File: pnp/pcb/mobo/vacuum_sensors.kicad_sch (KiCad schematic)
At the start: 18 parts, among them J33 I2C_AUX, U2 XGZP6857D, U3 XGZP6857D, U4 PCA9545A

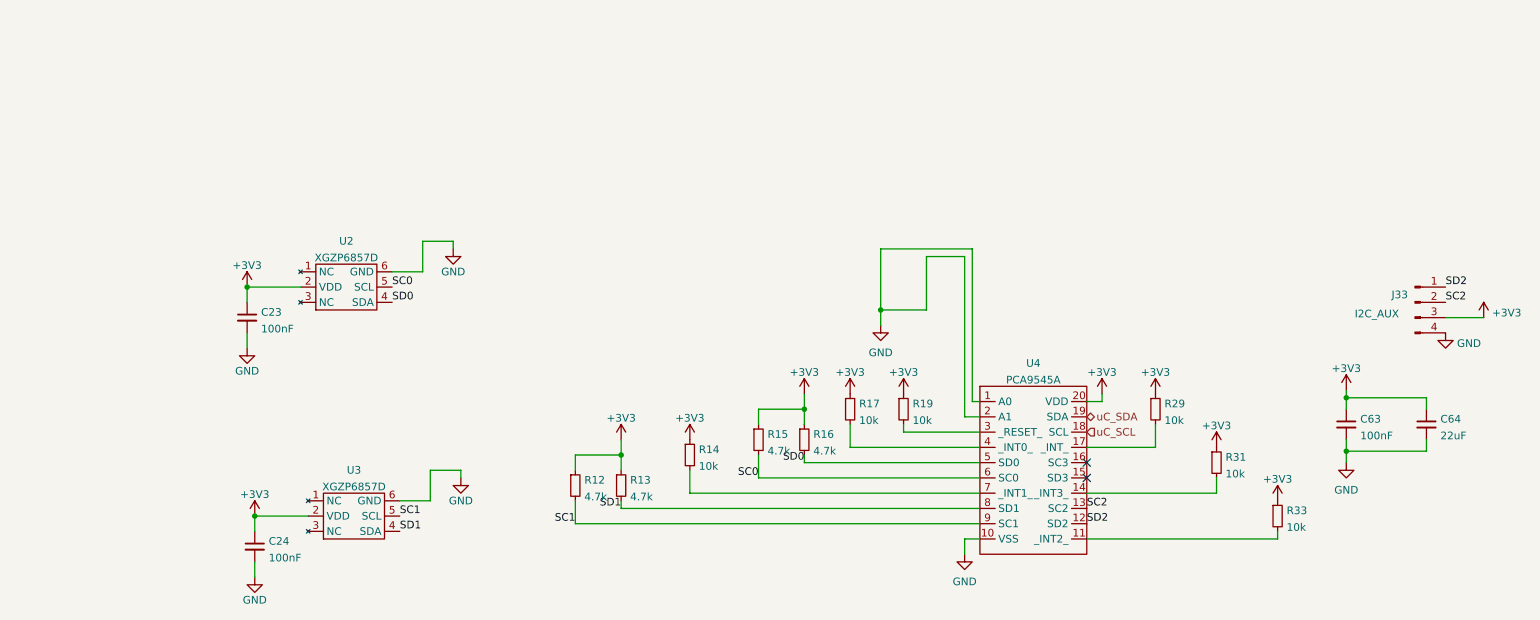
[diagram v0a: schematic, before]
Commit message: Update mobo schematic with part numbers and ratings
All parts now have part numbers for at least one reseller or manufacturer along with rating specifications.

Note: I did not update the PCB with these new properties, as it seems the PCB is a bit out of sync with the schematic.
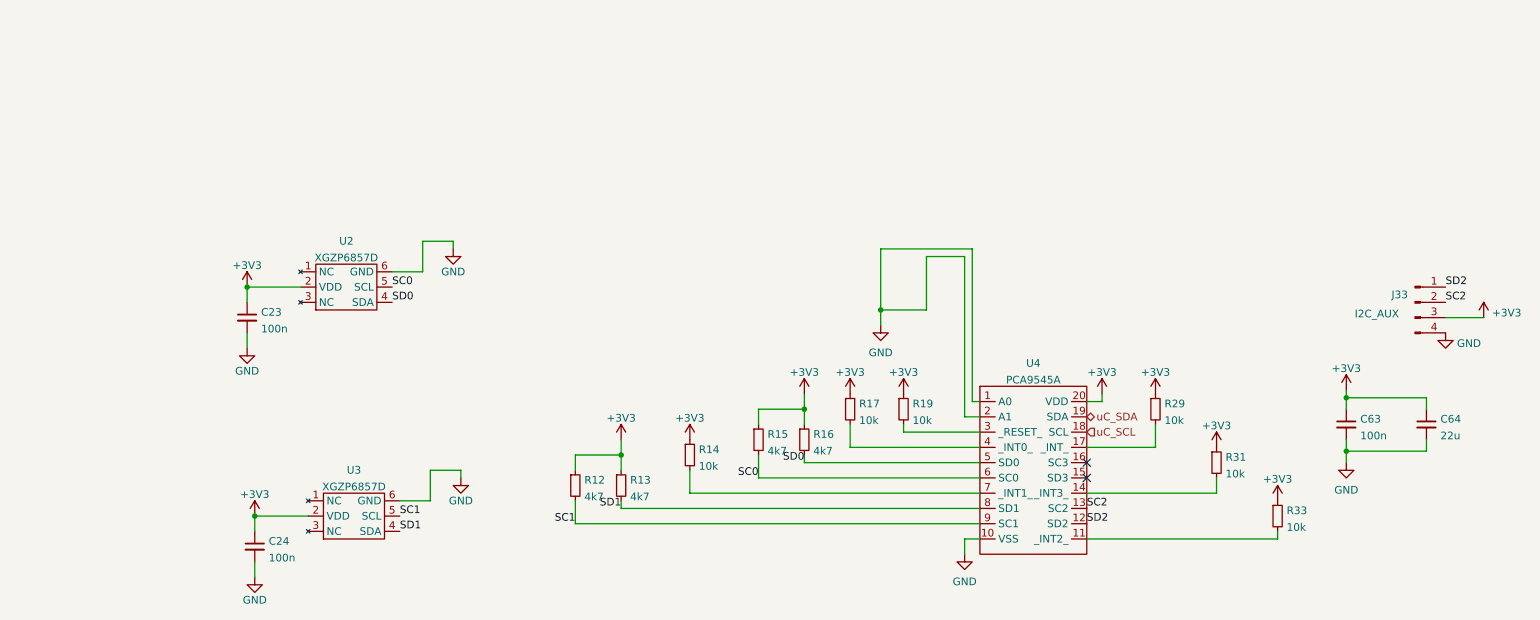
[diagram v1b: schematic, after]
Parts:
- C23, C24, C63: value 100nF -> 100n; Digikey (none) -> 1276-1180-1-ND; JLCPCB (none) -> C49678; LCSC (none) -> C360619; Mouser (none) -> 581-08055C104K; Notes (none) -> 50V/10%
- C64: value 22uF -> 22u; JLCPCB (none) -> C45783; LCSC (none) -> C5674; Notes (none) -> 25V/20%
- R12, R13, R15, R16: value 4.7k -> 4k7; Digikey (none) -> A129757CT-ND; JLCPCB (none) -> C17673; LCSC (none) -> C17673; Mouser (none) -> 71-CRCW08054K70FKEAC; Notes (none) -> 125mW/1%
- R14, R17, R19, R29, R31, R33: Digikey (none) -> RMCF0805FT10K0CT-ND; JLCPCB (none) -> C17414; LCSC (none) -> C115295; Mouser (none) -> 71-CRCW080510K0FKEAC; Notes (none) -> 125mW/1%
- U2, U3: Notes (none) -> Must at least cover 0 - 1 bar / 0 - 0.1 MPa / 0 - 15 PSI
- U4: Digikey (none) -> 568-1865-1-ND

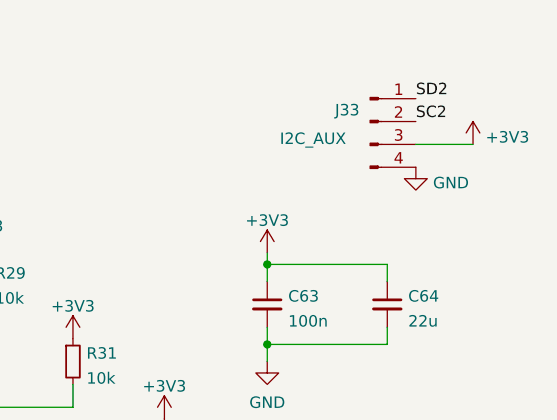
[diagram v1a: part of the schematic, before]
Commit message: adds tons of TVS and inline resistors
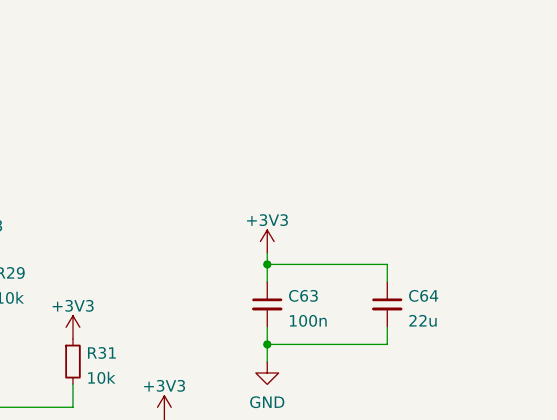
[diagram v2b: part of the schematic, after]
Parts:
- removed J33: I2C_AUX, Connector_PinHeader_2.54mm:PinHeader_1x04_P2.54mm_Vertical, symbol Connector:Conn_01x04_Male
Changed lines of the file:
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@@
-    (stroke (width 0) (type default))
-  )
-  (wire (pts (xy 261.62 88.9) (xy 267.97 88.9))
     (stroke (width 0) (type default))
   )
@@
     (effects (font (size 1.27 1.27)) (justify left bottom))
   )
-  (label "SD2" (at 261.62 83.82 0) (fields_autoplaced)
-    (effects (font (size 1.27 1.27)) (justify left bottom))
-  )
-  (label "SC2" (at 261.62 86.36 0) (fields_autoplaced)
-    (effects (font (size 1.27 1.27)) (justify left bottom))
-  )
   (label "SD0" (at 86.36 86.36 0) (fields_autoplaced)
     (effects (font (size 1.27 1.27)) (justify left bottom))
@@
     (effects (font (size 1.27 1.27)) (justify left))
   )
-  (symbol (lib_id "power:+3V3") (at 267.97 88.9 0) (unit 1)
-    (in_bom yes) (on_board yes) (dnp no) (fields_autoplaced)
-    (property "Reference" "#PWR0250" (at 267.97 92.71 0)
-      (effects (font (size 1.27 1.27)) hide)
-    )
-    (property "Value" "+3V3" (at 269.367 88.109 0)
-      (effects (font (size 1.27 1.27)) (justify left))
-    )
-    (property "Footprint" "" (at 267.97 88.9 0)
-      (effects (font (size 1.27 1.27)) hide)
-    )
-    (property "Datasheet" "" (at 267.97 88.9 0)
-      (effects (font (size 1.27 1.27)) hide)
-    )
-    (pin "1")
-    (instances
-      (project "mobo"
-        (path "/7255cbd1-8d38-4545-be9a-7fc5488ef942/00000000-0000-0000-0000-00005eb0c5a0"
-          (reference "#PWR0250") (unit 1)
-        )
-      )
-    )
-  )
   (symbol (lib_id "power:+3V3") (at 171.45 101.6 0) (unit 1)
     (in_bom yes) (on_board yes) (dnp no) (fields_autoplaced)
@@
         (path "/7255cbd1-8d38-4545-be9a-7fc5488ef942/00000000-0000-0000-0000-00005eb0c5a0"
           (reference "#PWR0241") (unit 1)
-        )
-      )
-    )
-  )
-  (symbol (lib_id "Connector:Conn_01x04_Male") (at 256.54 86.36 0) (unit 1)
-    (in_bom yes) (on_board yes) (dnp no)
-    (property "Reference" "J33" (at 254 85.09 0)
-      (effects (font (size 1.27 1.27)))
-    )
-    (property "Value" "I2C_AUX" (at 250.19 88.265 0)
-      (effects (font (size 1.27 1.27)))
-    )
-    (property "Footprint" "Connector_PinHeader_2.54mm:PinHeader_1x04_P2.54mm_Vertical" (at 256.54 86.36 0)
-      (effects (font (size 1.27 1.27)) hide)
-    )
-    (property "Datasheet" "~" (at 256.54 86.36 0)
-      (effects (font (size 1.27 1.27)) hide)
-    )
-    (pin "1")
-    (pin "2")
-    (pin "3")
-    (pin "4")
-    (instances
-      (project "mobo"
-        (path "/7255cbd1-8d38-4545-be9a-7fc5488ef942/00000000-0000-0000-0000-00005eb0c5a0"
-          (reference "J33") (unit 1)
         )
       )
@@
         )
       )
-    )
-  )
-  (symbol (lib_id "power:GND") (at 261.62 91.44 0) (unit 1)
-    (in_bom yes) (on_board yes) (dnp no) (fields_autoplaced)
-    (property "Reference" "#PWR0249" (at 261.62 97.79 0)
-      (effects (font (size 1.27 1.27)) hide)
-    )
-    (property "Value" "GND" (at 263.525 93.189 0)
-      (effects (font (size 1.27 1.27)) (justify left))
-    )
-    (property "Footprint" "" (at 261.62 91.44 0)
-      (effects (font (size 1.27 1.27)) hide)
-    )
-    (property "Datasheet" "" (at 261.62 91.44 0)
-      (effects (font (size 1.27 1.27)) hide)
-    )
-    (pin "1")
-    (instances
-      (project "mobo"
-        (path "/7255cbd1-8d38-4545-be9a-7fc5488ef942/00000000-0000-0000-0000-00005eb0c5a0"
-          (reference "#PWR0249") (unit 1)
-        )
-      )

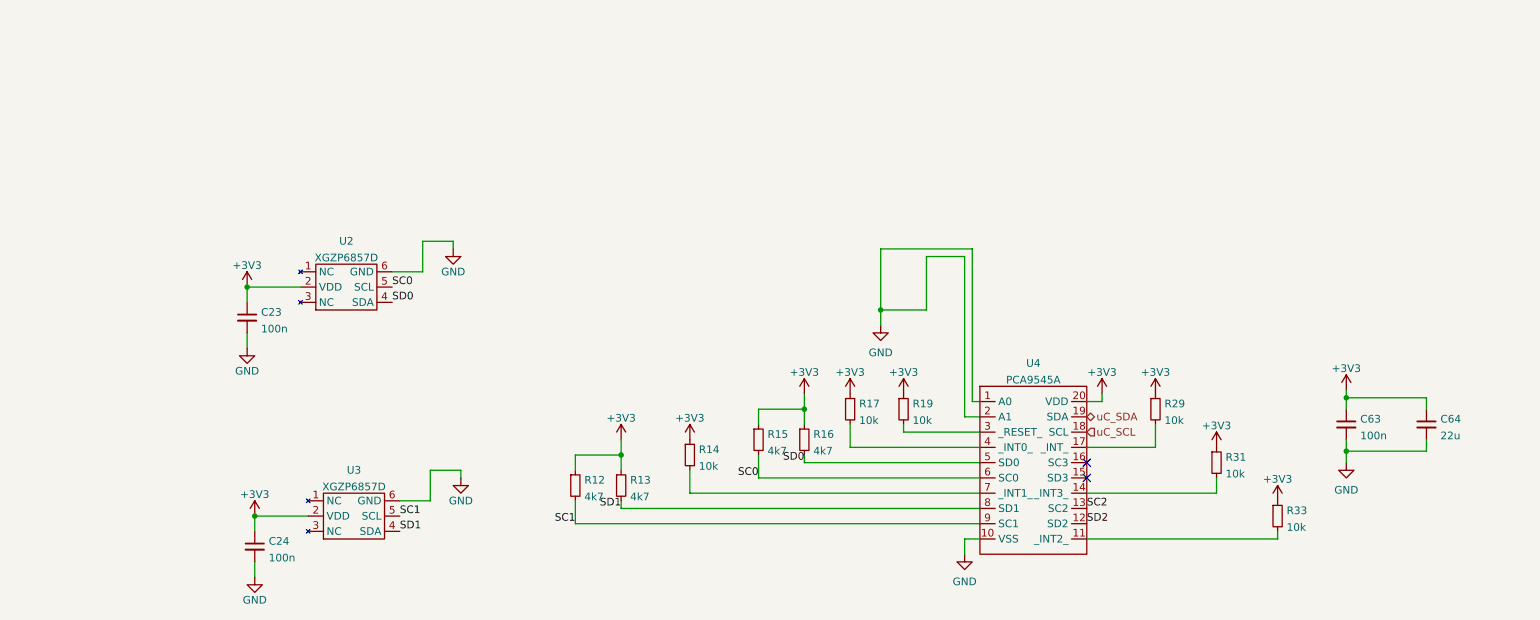
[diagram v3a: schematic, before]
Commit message: Updated symbols and changed I2C multiplexer to a simpler one
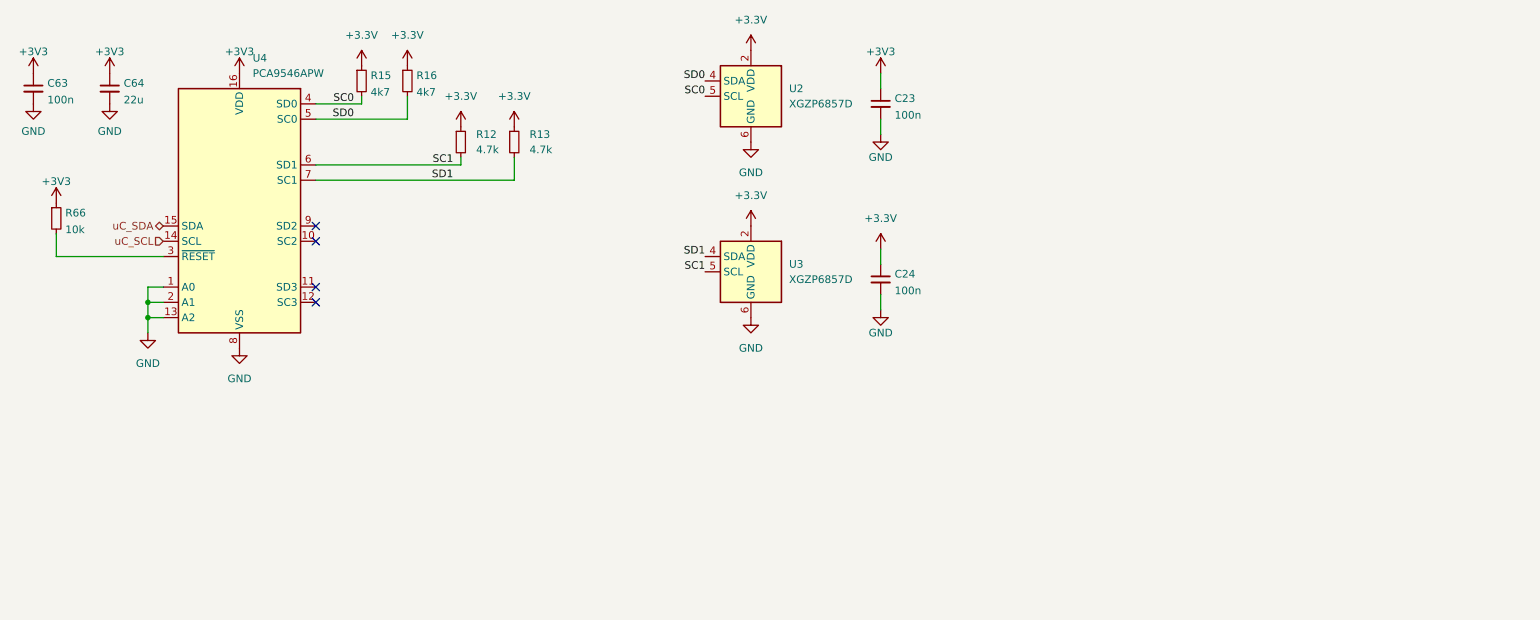
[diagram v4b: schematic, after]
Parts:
- removed R14, R17, R19, R29, R31, R33: 10k, Resistor_SMD:R_0805_2012Metric, symbol Device:R_Small
- removed U4: PCA9545A, Package_SO:TSSOP-20_4.4x6.5mm_P0.65mm, symbol index:PCA9545A
- added R66: 10k, Resistor_SMD:R_0805_2012Metric, symbol Device:R_Small
- added U4: PCA9546APW, Package_SO:TSSOP-16_4.4x5mm_P0.65mm, symbol index:PCA9546APW
- R12, R13: value 4k7 -> 4.7k
- U2, U3: footprint index:XGZP6857D -> Package_DIP:DIP-6_W10.16mm; Notes Must at least cover 0 - 1 bar / 0 - 0.1 MPa / 0 - 15 PSI -> (none)
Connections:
- net +3V3: now also R66.1, U4.16 (VDD); no longer C24.1, R12.1, R13.1, R15.1, R16.1, U2.2 (VDD), U3.2 (VDD)
- net GND: now also U4.1 (A0), U4.13 (A2), U4.2 (A1), U4.8 (VSS)
- net SC0: now also U4.4 (SD0)
- net SC1: now also U4.6 (SD1)
- net SD0: now also U4.5 (SC0)
- net SD1: now also U4.7 (SC1)
- net uC_SCL: now also U4.14 (SCL)
- net uC_SDA: now also U4.15 (SDA)
- new net: R66.2, U4.3 (~{RESET})
- new net +3.3V: C24.1, R12.1, R13.1, R15.1, R16.1, U2.2 (VDD), U3.2 (VDD)
- no-connect marks 2 -> 4
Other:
- moved on the sheet: C23, C24, C63, C64, R12, R13

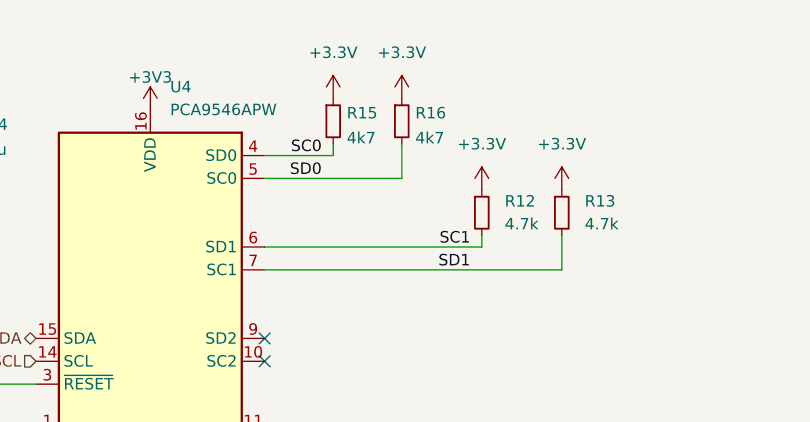
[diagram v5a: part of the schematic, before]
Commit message: Move level shifting from ringlight to mobo
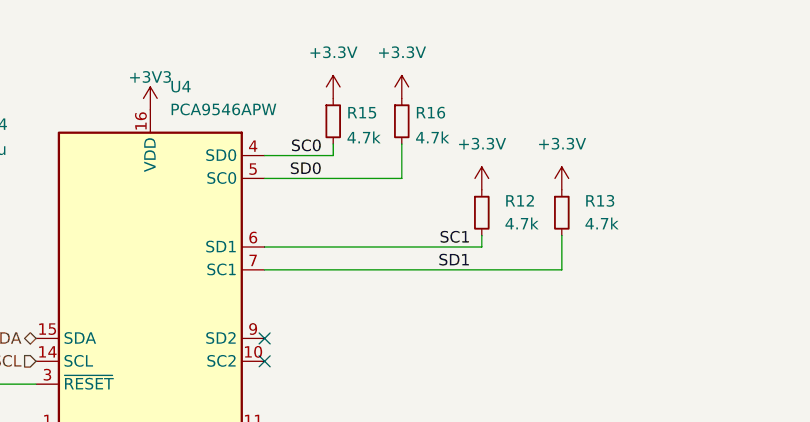
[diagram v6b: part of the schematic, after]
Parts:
- R15, R16: value 4k7 -> 4.7k
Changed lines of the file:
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@@
       (effects (font (size 1.27 1.27)) (justify left))
     )
-    (property "Value" "4k7" (at 90.3986 51.3966 0)
+    (property "Value" "4.7k" (at 90.3986 51.3966 0)
       (effects (font (size 1.27 1.27)) (justify left))
     )
@@
       (effects (font (size 1.27 1.27)) (justify left))
     )
-    (property "Value" "4k7" (at 82.7786 51.3966 0)
-      (effects (font (size 1.27 1.27)) (justify left))
-    )
+    (property "Value" "4.7k" (at 82.7786 51.3966 0)
+      (effects (font (size 1.27 1.27)) (justify left))
+    )

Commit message: Mobo parts sourced
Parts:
- C23, C24, C63: Digikey 1276-1180-1-ND -> (none); LCSC C360619 -> C476766; Mouser 581-08055C104K -> (none); Notes 50V/10% -> 6.3V
- C64: JLCPCB C45783 -> C1729; LCSC C5674 -> C107147; Notes 25V/20% -> 6.3V
- R12, R13, R15, R16: Notes 125mW/1% -> (none)
- R66: LCSC C115295 -> C17414; Notes 125mW/1% -> (none)
- U2, U3: JLCPCB (none) -> C3038044; LCSC (none) -> C3038044
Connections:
- net +3V3 is gone; now on net +3.3V: C23.1, C63.1, C64.1, R66.1, U4.16 (VDD)

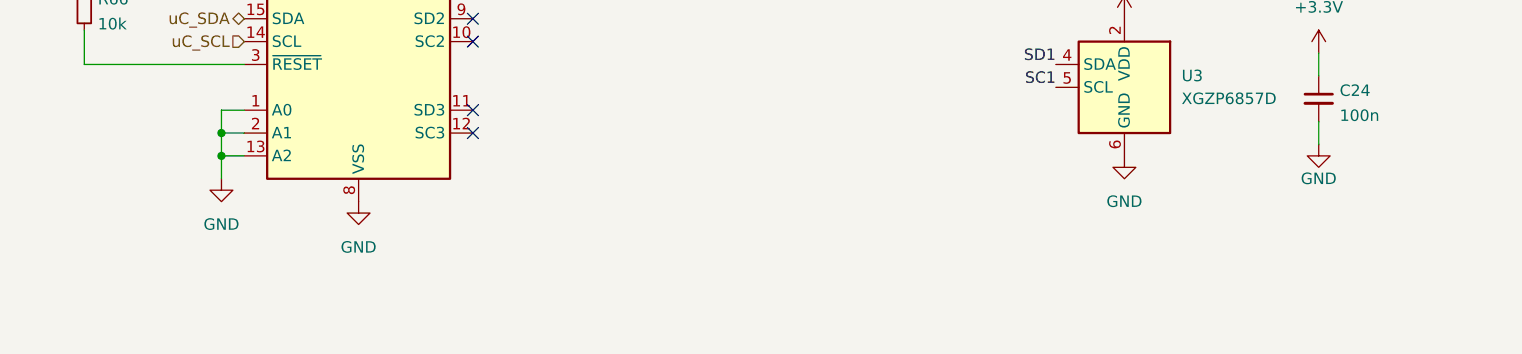
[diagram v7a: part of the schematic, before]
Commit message: Add notes to pending symbols
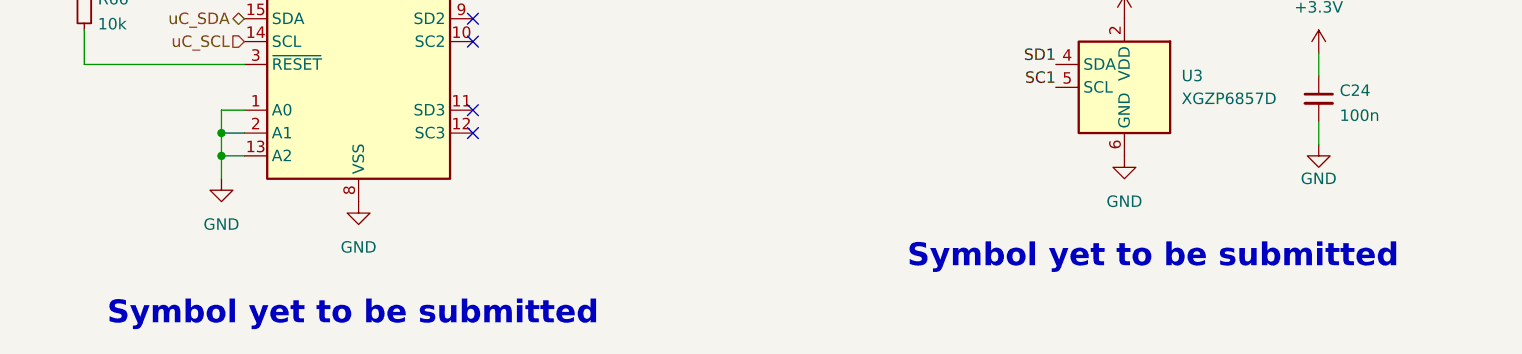
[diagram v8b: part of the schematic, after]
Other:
- note added: "Symbol yet to be submitted"
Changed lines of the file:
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@@
     (stroke (width 0) (type default))
+  )
+  (text "Symbol yet to be submitted" (at 121.92 101.6 0)
+    (effects (font (size 2.54 2.54) (thickness 0.508) bold) (justify left bottom))
+  )
+  (text "Symbol yet to be submitted" (at 33.02 107.95 0)
+    (effects (font (size 2.54 2.54) (thickness 0.508) bold) (justify left bottom))
   )
   (label "SD1" (at 138.43 78.74 180) (fields_autoplaced)
